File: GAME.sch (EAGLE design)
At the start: 33 parts, among them J1 Digital_0_7, J2 Analog, J3 Digital_8_13, J4 Power, J5 ICSP, J6 M05X2PTH

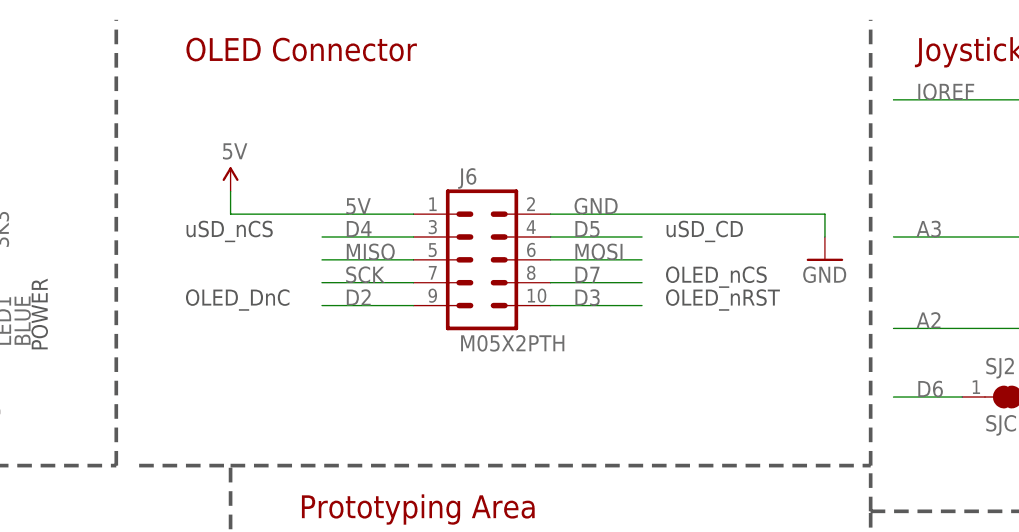
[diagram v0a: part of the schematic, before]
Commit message: Fixed OLED pinout for v1.1 release
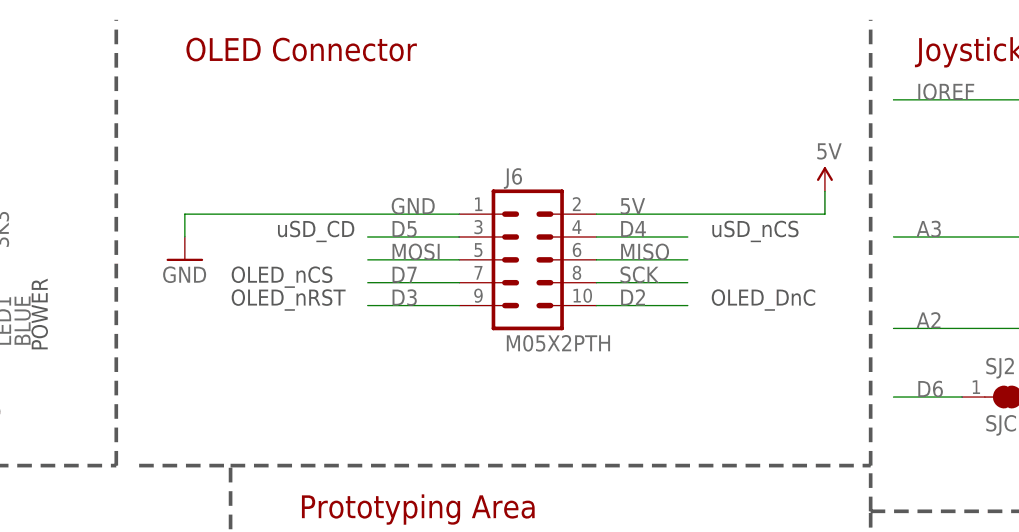
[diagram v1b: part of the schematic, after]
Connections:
- net 5V: now also J6.2; no longer J6.1
- net D2: now also J6.10; no longer J6.9
- net D3: now also J6.9; no longer J6.10
- net D4: now also J6.4; no longer J6.3
- net D5: now also J6.3; no longer J6.4
- net D7: now also J6.7; no longer J6.8
- net GND: now also J6.1; no longer J6.2
- net MISO: now also J6.6; no longer J6.5
- net MOSI: now also J6.5; no longer J6.6
- net SCK: now also J6.8; no longer J6.7
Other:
- moved on the sheet: J6
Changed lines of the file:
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@@
 <wire x1="116.84" y1="132.08" x2="116.84" y2="181.61" width="0.4064" layer="97" style="longdash"/>
 <wire x1="45.72" y1="101.6" x2="45.72" y2="132.08" width="0.4064" layer="97" style="longdash"/>
-<text x="40.64" y="149.86" size="1.778" layer="97">OLED_DnC</text>
-<text x="93.98" y="157.48" size="1.778" layer="97">uSD_CD</text>
-<text x="93.98" y="152.4" size="1.778" layer="97">OLED_nCS</text>
-<text x="93.98" y="149.86" size="1.778" layer="97">OLED_nRST</text>
-<text x="40.64" y="157.48" size="1.778" layer="97">uSD_nCS</text>
+<text x="99.06" y="149.86" size="1.778" layer="97">OLED_DnC</text>
+<text x="50.8" y="157.48" size="1.778" layer="97">uSD_CD</text>
+<text x="45.72" y="152.4" size="1.778" layer="97">OLED_nCS</text>
+<text x="45.72" y="149.86" size="1.778" layer="97">OLED_nRST</text>
+<text x="99.06" y="157.48" size="1.778" layer="97">uSD_nCS</text>
 <wire x1="175.26" y1="93.98" x2="175.26" y2="127" width="0.4064" layer="97" style="longdash"/>
 <wire x1="175.26" y1="127" x2="175.26" y2="181.61" width="0.4064" layer="97" style="longdash"/>
@@
 <instance part="S1" gate="S" x="210.82" y="157.48"/>
 <instance part="S4" gate="S" x="210.82" y="111.76"/>
-<instance part="J6" gate="G$1" x="73.66" y="154.94"/>
-<instance part="GND2" gate="1" x="111.76" y="154.94"/>
-<instance part="U$2" gate="G$1" x="45.72" y="162.56"/>
+<instance part="J6" gate="G$1" x="78.74" y="154.94"/>
+<instance part="GND2" gate="1" x="40.64" y="154.94"/>
+<instance part="U$2" gate="G$1" x="111.76" y="162.56"/>
 <instance part="U$3" gate="G$1" x="17.78" y="167.64"/>
 <instance part="PIEZO1" gate="G$1" x="154.94" y="114.3" smashed="yes" rot="MR90">
@@
 </segment>
 <segment>
-<pinref part="J6" gate="G$1" pin="1"/>
-<wire x1="66.04" y1="160.02" x2="45.72" y2="160.02" width="0.1524" layer="91"/>
-<label x="58.42" y="160.02" size="1.778" layer="95"/>
-<pinref part="U$2" gate="G$1" pin="5V"/>
-<wire x1="45.72" y1="160.02" x2="45.72" y2="162.56" width="0.1524" layer="91"/>
-</segment>
-<segment>
 <pinref part="R1" gate="G$1" pin="2"/>
 <wire x1="17.78" y1="165.1" x2="17.78" y2="167.64" width="0.1524" layer="91"/>
@@
 <pinref part="U$1" gate="G$1" pin="5V"/>
 <wire x1="147.32" y1="20.32" x2="147.32" y2="22.86" width="0.1524" layer="91"/>
+</segment>
+<segment>
+<pinref part="J6" gate="G$1" pin="2"/>
+<wire x1="86.36" y1="160.02" x2="111.76" y2="160.02" width="0.1524" layer="91"/>
+<label x="88.9" y="160.02" size="1.778" layer="95"/>
+<pinref part="U$2" gate="G$1" pin="5V"/>
+<wire x1="111.76" y1="160.02" x2="111.76" y2="162.56" width="0.1524" layer="91"/>
 </segment>
 </net>
@@
 </segment>
 <segment>
-<pinref part="GND2" gate="1" pin="GND"/>
-<wire x1="111.76" y1="157.48" x2="111.76" y2="160.02" width="0.1524" layer="91"/>
-<pinref part="J6" gate="G$1" pin="2"/>
-<wire x1="81.28" y1="160.02" x2="111.76" y2="160.02" width="0.1524" layer="91"/>
-<label x="83.82" y="160.02" size="1.778" layer="95"/>
-</segment>
-<segment>
 <wire x1="147.32" y1="114.3" x2="149.86" y2="114.3" width="0.1524" layer="91"/>
 <pinref part="PIEZO1" gate="G$1" pin="1"/>
@@
 <wire x1="147.32" y1="160.02" x2="147.32" y2="149.86" width="0.1524" layer="91"/>
 </segment>
+<segment>
+<pinref part="J6" gate="G$1" pin="1"/>
+<wire x1="71.12" y1="160.02" x2="40.64" y2="160.02" width="0.1524" layer="91"/>
+<label x="63.5" y="160.02" size="1.778" layer="95"/>
+<pinref part="GND2" gate="1" pin="GND"/>
+<wire x1="40.64" y1="160.02" x2="40.64" y2="157.48" width="0.1524" layer="91"/>
+</segment>
 </net>
 <net name="VIN" class="0">
@@
 </segment>
 <segment>
-<pinref part="J6" gate="G$1" pin="8"/>
-<wire x1="81.28" y1="152.4" x2="91.44" y2="152.4" width="0.1524" layer="91"/>
-<label x="83.82" y="152.4" size="1.778" layer="95"/>
+<pinref part="J6" gate="G$1" pin="7"/>
+<wire x1="71.12" y1="152.4" x2="60.96" y2="152.4" width="0.1524" layer="91"/>
+<label x="63.5" y="152.4" size="1.778" layer="95"/>
 </segment>
 </net>
@@
 </segment>
 <segment>
-<pinref part="J6" gate="G$1" pin="4"/>
-<wire x1="81.28" y1="157.48" x2="91.44" y2="157.48" width="0.1524" layer="91"/>
-<label x="83.82" y="157.48" size="1.778" layer="95"/>
+<pinref part="J6" gate="G$1" pin="3"/>
+<wire x1="71.12" y1="157.48" x2="60.96" y2="157.48" width="0.1524" layer="91"/>
+<label x="63.5" y="157.48" size="1.778" layer="95"/>
 </segment>
 </net>
@@
 </segment>
 <segment>
-<pinref part="J6" gate="G$1" pin="3"/>
-<wire x1="66.04" y1="157.48" x2="55.88" y2="157.48" width="0.1524" layer="91"/>
-<label x="58.42" y="157.48" size="1.778" layer="95"/>
+<pinref part="J6" gate="G$1" pin="4"/>
+<wire x1="86.36" y1="157.48" x2="96.52" y2="157.48" width="0.1524" layer="91"/>
+<label x="88.9" y="157.48" size="1.778" layer="95"/>
 </segment>
 </net>
@@
 </segment>
 <segment>
-<pinref part="J6" gate="G$1" pin="10"/>
-<wire x1="81.28" y1="149.86" x2="91.44" y2="149.86" width="0.1524" layer="91"/>
-<label x="83.82" y="149.86" size="1.778" layer="95"/>
+<pinref part="J6" gate="G$1" pin="9"/>
+<wire x1="71.12" y1="149.86" x2="60.96" y2="149.86" width="0.1524" layer="91"/>
+<label x="63.5" y="149.86" size="1.778" layer="95"/>
 </segment>
 </net>
@@
 </segment>
 <segment>
-<pinref part="J6" gate="G$1" pin="9"/>
-<wire x1="66.04" y1="149.86" x2="55.88" y2="149.86" width="0.1524" layer="91"/>
-<label x="58.42" y="149.86" size="1.778" layer="95"/>
+<pinref part="J6" gate="G$1" pin="10"/>
+<wire x1="86.36" y1="149.86" x2="96.52" y2="149.86" width="0.1524" layer="91"/>
+<label x="88.9" y="149.86" size="1.778" layer="95"/>
 </segment>
 </net>
@@
 <net name="MISO" class="0">
 <segment>
-<pinref part="J6" gate="G$1" pin="5"/>
-<wire x1="66.04" y1="154.94" x2="55.88" y2="154.94" width="0.1524" layer="91"/>
-<label x="58.42" y="154.94" size="1.778" layer="95"/>
-</segment>
-<segment>
 <pinref part="J5" gate="G$1" pin="1"/>
 <wire x1="124.46" y1="20.32" x2="116.84" y2="20.32" width="0.1524" layer="91"/>
 <label x="116.84" y="20.32" size="1.778" layer="95"/>
 </segment>
+<segment>
+<pinref part="J6" gate="G$1" pin="6"/>
+<wire x1="86.36" y1="154.94" x2="96.52" y2="154.94" width="0.1524" layer="91"/>
+<label x="88.9" y="154.94" size="1.778" layer="95"/>
+</segment>
 </net>
 <net name="SCK" class="0">
-<segment>
-<pinref part="J6" gate="G$1" pin="7"/>
-<wire x1="66.04" y1="152.4" x2="55.88" y2="152.4" width="0.1524" layer="91"/>
-<label x="58.42" y="152.4" size="1.778" layer="95"/>
-</segment>
 <segment>
 <pinref part="J5" gate="G$1" pin="3"/>
@@
 <label x="116.84" y="17.78" size="1.778" layer="95"/>
 </segment>
+<segment>
+<pinref part="J6" gate="G$1" pin="8"/>
+<wire x1="86.36" y1="152.4" x2="96.52" y2="152.4" width="0.1524" layer="91"/>
+<label x="88.9" y="152.4" size="1.778" layer="95"/>
+</segment>
 </net>
 <net name="MOSI" class="0">
-<segment>
-<pinref part="J6" gate="G$1" pin="6"/>
-<wire x1="81.28" y1="154.94" x2="91.44" y2="154.94" width="0.1524" layer="91"/>
-<label x="83.82" y="154.94" size="1.778" layer="95"/>
-</segment>
 <segment>
 <pinref part="J5" gate="G$1" pin="4"/>
@@
 <label x="144.78" y="17.78" size="1.778" layer="95"/>
 </segment>
-</net>
+<segment>
+<pinref part="J6" gate="G$1" pin="5"/>
+<wire x1="71.12" y1="154.94" x2="60.96" y2="154.94" width="0.1524" layer="91"/>
+<label x="63.5" y="154.94" size="1.778" layer="95"/>
+</segment>
+</net>
